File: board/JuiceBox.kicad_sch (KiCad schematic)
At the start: 33 parts, among them J1 USB_C_Receptacle_USB2.0, SW1 SW_SPST, SW10 SW_SPST, SW11 SW_SPST, SW12 SW_SPST, SW2 SW_SPST, SW3 SW_SPST, SW4 SW_SPST, SW5 SW_SPST, SW6 SW_SPST, SW7 SW_SPST, SW8 SW_SPST, SW9 SW_SPST, U1 ATmega8U2-A

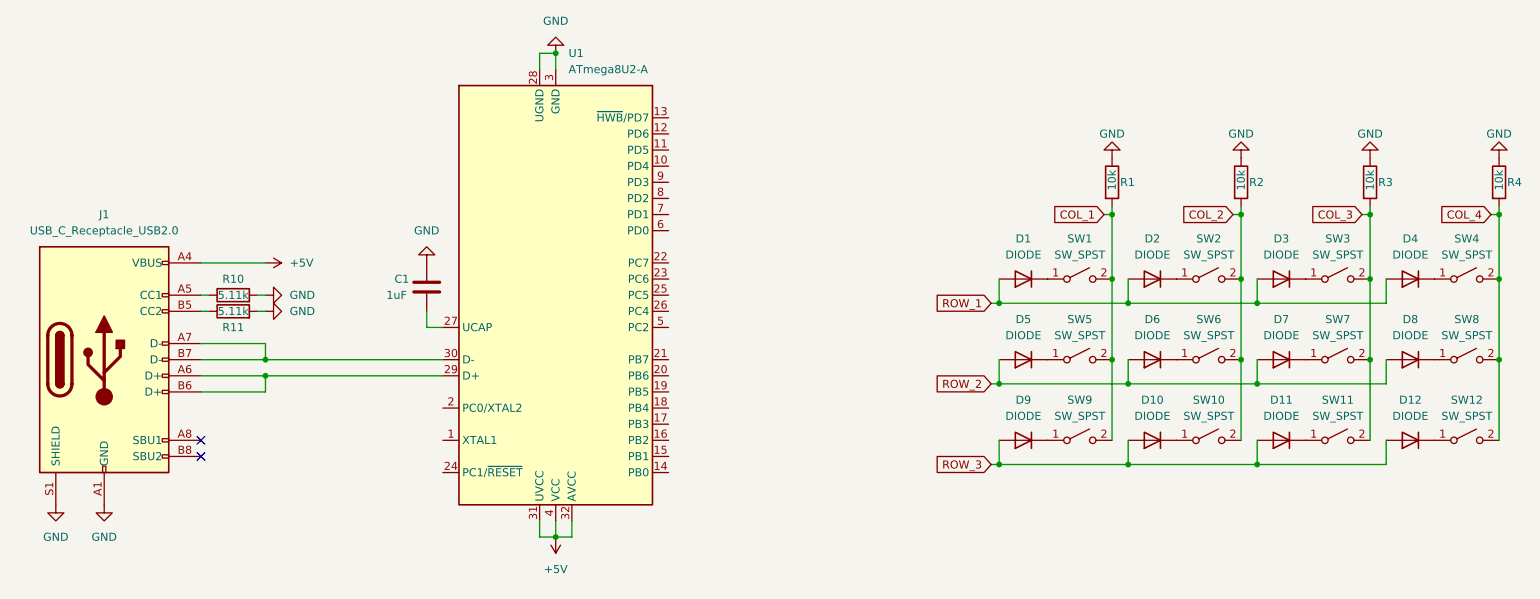
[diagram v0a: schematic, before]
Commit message: add crystal for usb operation
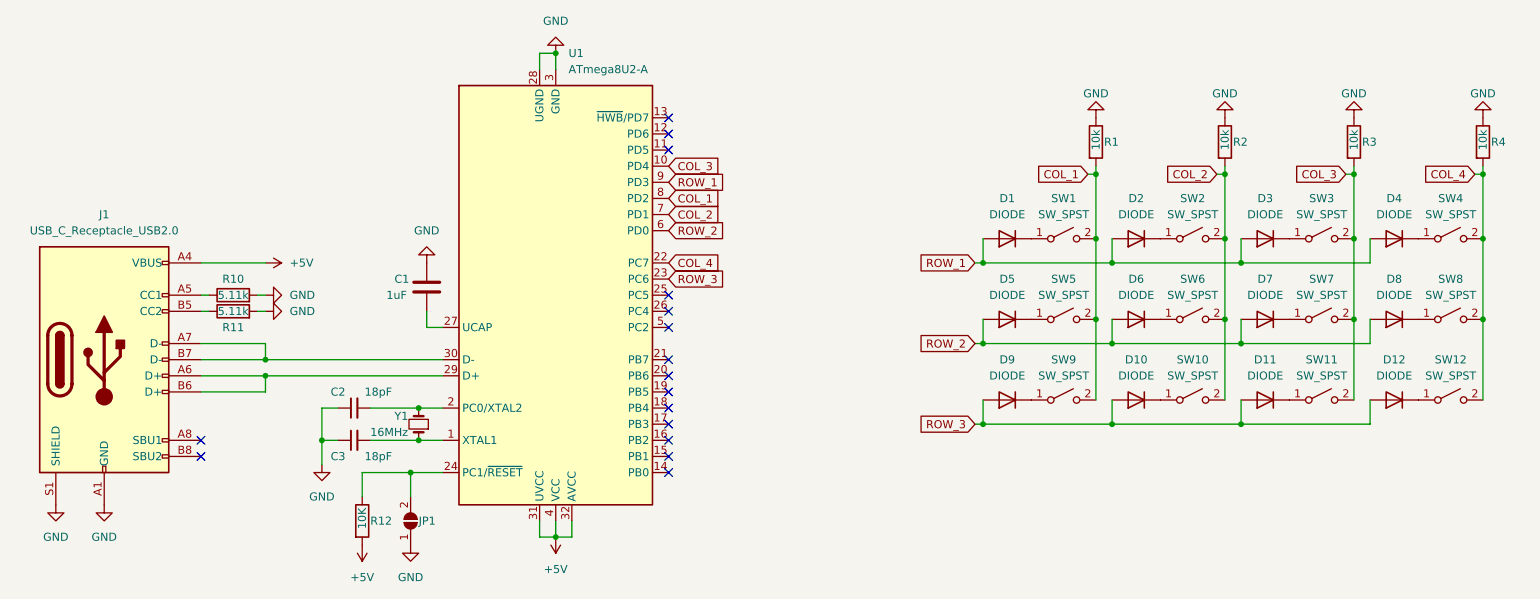
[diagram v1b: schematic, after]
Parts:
- added C2, C3: 18pF, symbol Device:C_Small
- added JP1: (no value), symbol Jumper:SolderJumper_2_Open
- added R12: 10K, symbol Device:R
- added Y1: 16MHz, symbol Device:Crystal_Small
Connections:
- net +5V: now also R12.2
- net COL_1: now also U1.8 (PD2)
- net COL_2: now also U1.7 (PD1)
- net COL_3: now also U1.10 (PD4)
- net COL_4: now also U1.22 (PC7)
- net GND: now also C2.1, C3.1, JP1.1 (A)
- net ROW_1: now also U1.9 (PD3)
- net ROW_2: now also U1.6 (PD0)
- net ROW_3: now also U1.23 (PC6)
- net at U1.1 (XTAL1): now also C3.2, Y1.1
- net at U1.2 (PC0/XTAL2): now also C2.2, Y1.2
- net at U1.24 (PC1/~{RESET}): now also JP1.2 (B), R12.1
- no-connect marks 2 -> 16
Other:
- moved on the sheet: D1, D10, D11, D12, D2, D3, D4, D5, D6, D7, D8, D9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

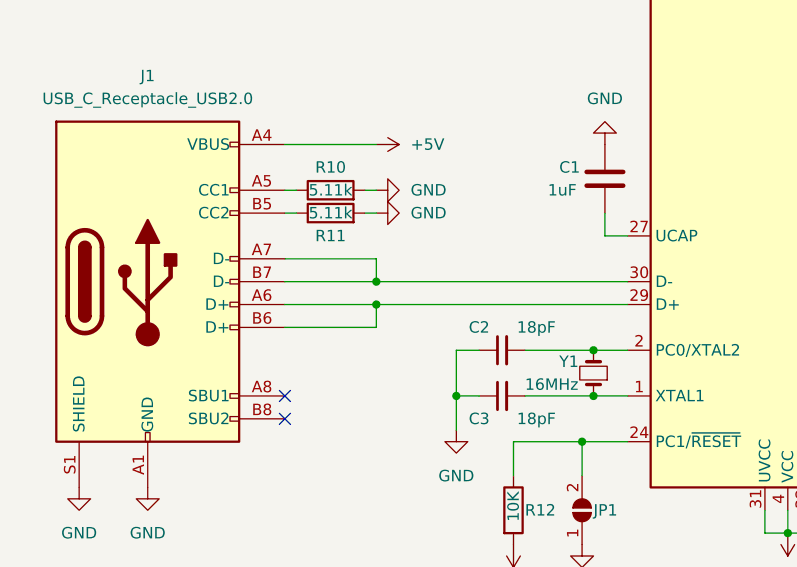
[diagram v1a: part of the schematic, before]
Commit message: add usb c connector, connect everything together
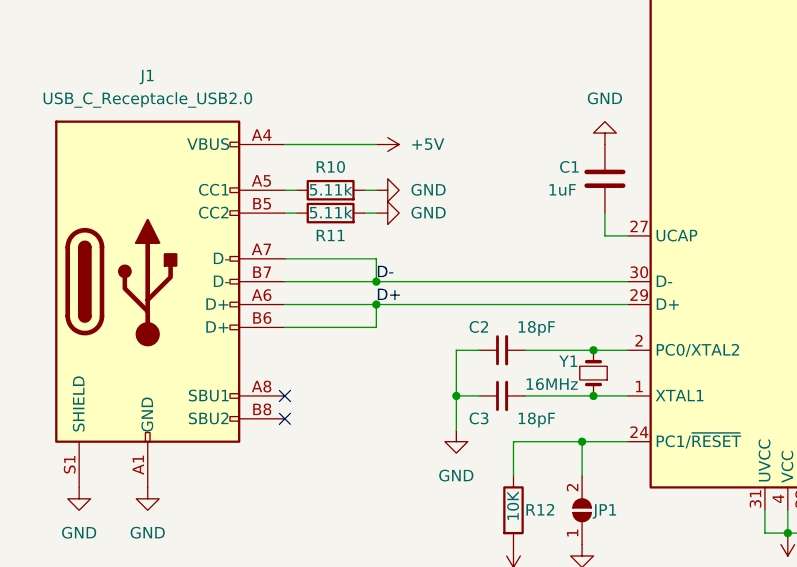
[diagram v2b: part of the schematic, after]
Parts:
- C1, C2, C3: footprint (none) -> Capacitor_SMD:C_0805_2012Metric_Pad1.18x1.45mm_HandSolder
- D1, D10, D11, D12, D2, D3, D4, D5, D6, D7, D8, D9: footprint (none) -> Diode_SMD:D_0805_2012Metric_Pad1.15x1.40mm_HandSolder
- J1: footprint (none) -> USB4085-GF-A:GCT_USB4085-GF-A_REVA4
- JP1: footprint (none) -> Jumper:SolderJumper-2_P1.3mm_Open_Pad1.0x1.5mm
- R1, R10, R11, R12, R2, R3, R4: footprint (none) -> Resistor_SMD:R_0805_2012Metric_Pad1.20x1.40mm_HandSolder
- SW1, SW10, SW11, SW12, SW2, SW3, SW4, SW5, SW6, SW7, SW8, SW9: footprint (none) -> Button_Switch_Keyboard:SW_Cherry_MX_1.00u_PCB
- Y1: footprint (none) -> Crystal:Crystal_HC18-U_Vertical
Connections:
- net D+: now reaches J1.A6 (D+), J1.B6 (D+), U1.29 (D+)
- net D-: now reaches J1.A7 (D-), J1.B7 (D-), U1.30 (D-)

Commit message: move all components to top, all throughhole
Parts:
- C1, C2, C3: footprint Capacitor_SMD:C_0805_2012Metric_Pad1.18x1.45mm_HandSolder -> Capacitor_THT:C_Disc_D5.0mm_W2.5mm_P5.00mm
- D1, D10, D11, D12, D2, D3, D4, D5, D6, D7, D8, D9: footprint Diode_SMD:D_0805_2012Metric_Pad1.15x1.40mm_HandSolder -> Diode_THT:D_DO-15_P10.16mm_Horizontal
- R1, R10, R11, R12, R2, R3, R4: footprint Resistor_SMD:R_0805_2012Metric_Pad1.20x1.40mm_HandSolder -> Resistor_THT:R_Axial_DIN0207_L6.3mm_D2.5mm_P10.16mm_Horizontal
